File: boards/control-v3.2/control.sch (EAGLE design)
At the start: 111 parts, among them IC1 MCP23017-E/SS, J1 2-PIN-KICKERS, J3 HFW8R-1ST, J4 4-PIN-HEADER, J6 DF22-2, Q1 BSS806NH6327XTSA1, Q2 BSS806NH6327XTSA1, U1 XC3S250E-4TQG144C, U11 MCP1824T-1202E/OT, U12 MCP1824T-2502E/OT, U13 TLV70233DBVR, U4 ICM-42605, U5 SN74AHC1G125, U7 MPM3620GQV-P, U8 VND5E006ASPTR-E, X1 ASV-18.432MHZ-EJ-T

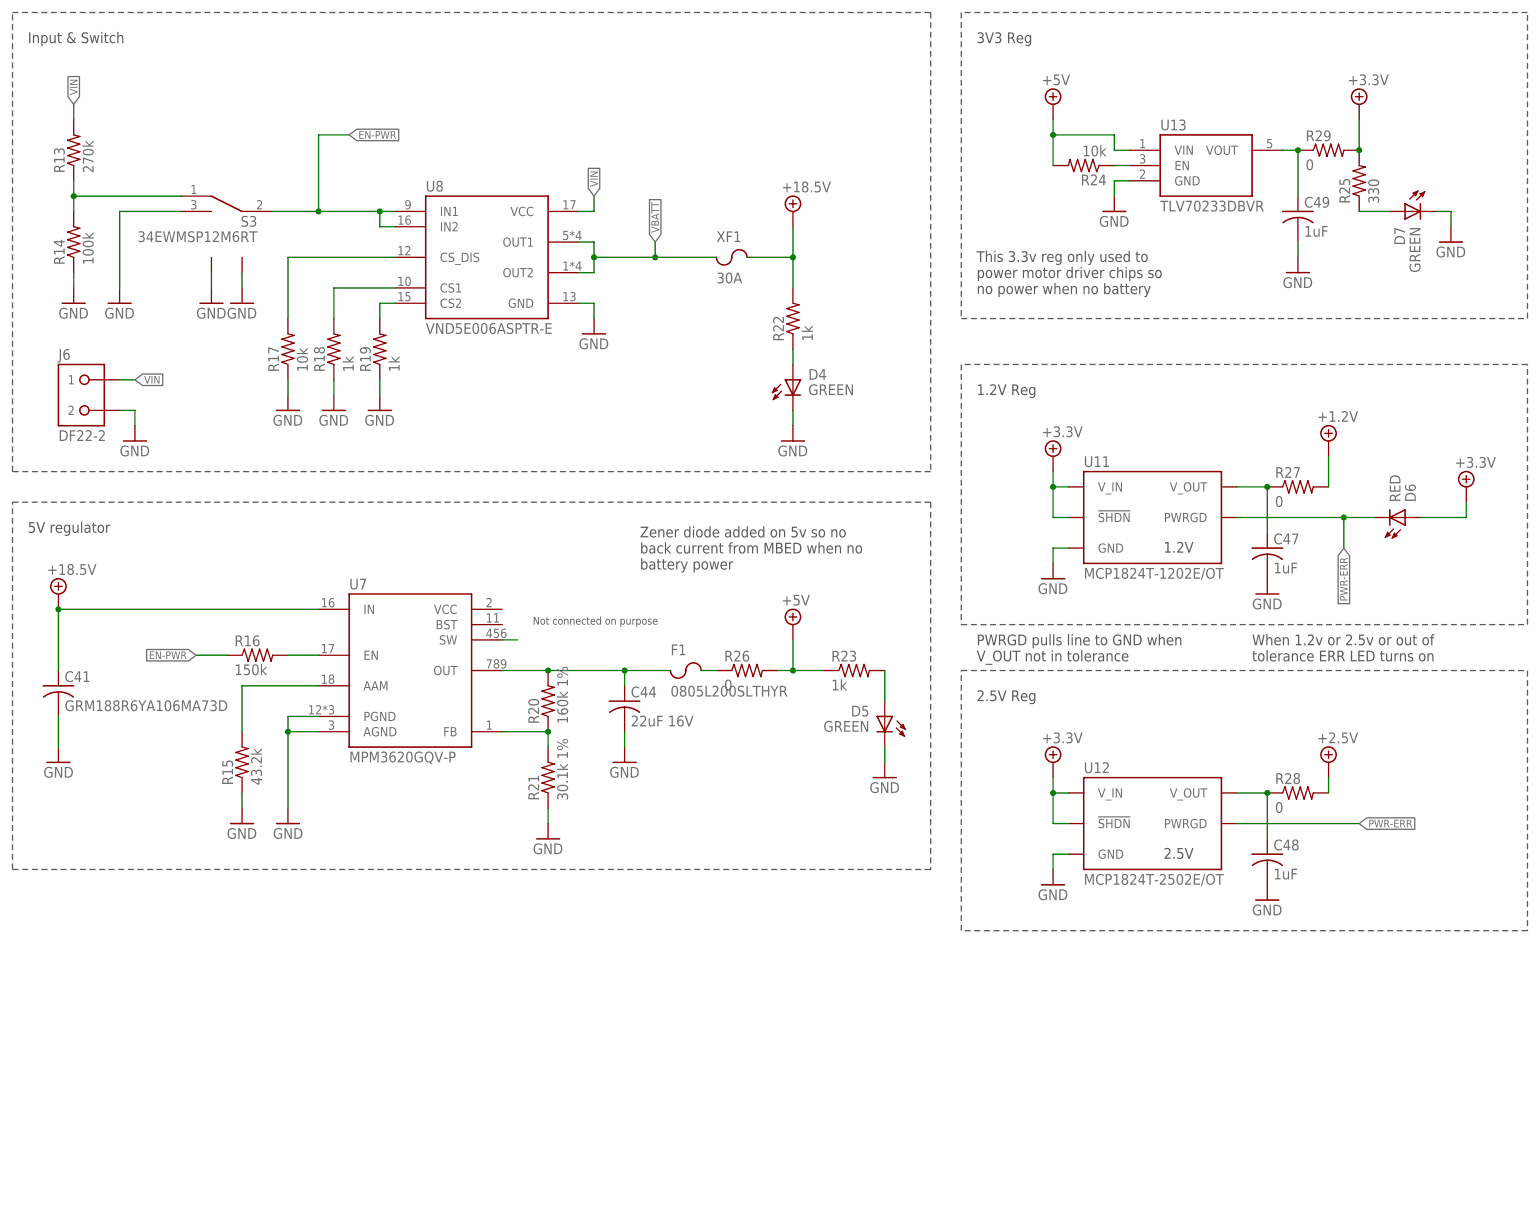
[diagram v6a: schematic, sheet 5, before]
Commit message: updated 3v3 reg
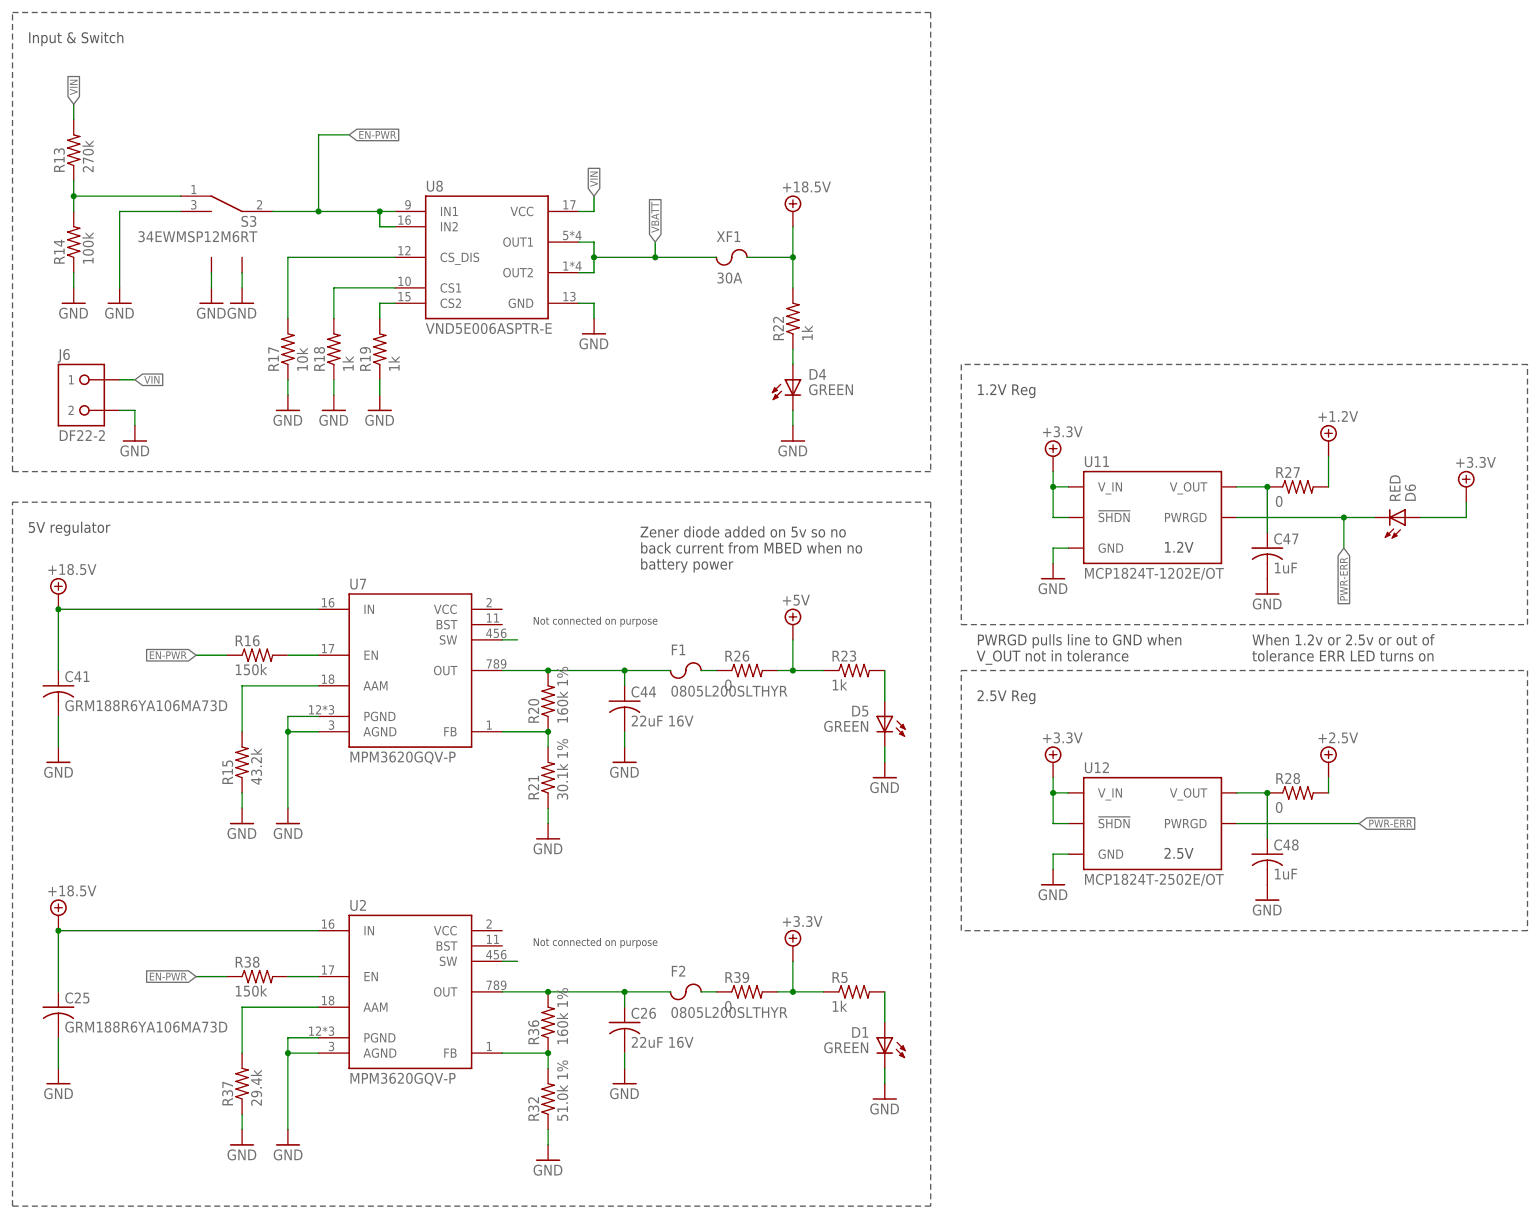
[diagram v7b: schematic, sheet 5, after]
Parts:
- removed C49: 1uF, rcl:C-USC0603
- removed D7: GREEN, RoboJackets-LEDs:LED-SMD-GREEN
- removed R24: 10k, rcl:R-US_R0603
- removed R25: 330, resistor:R-US_R0603
- removed R29: 0, resistor:R-US_R0603
- removed U13: TLV70233DBVR, RoboJackets-PowerICs:TLV70233DBVR
- added C25: GRM188R6YA106MA73D, rcl:C-USC0603
- added C26: 22uF 16V, rcl:C-USC0805
- added D1: GREEN, RoboJackets-LEDs:LED-SMD-GREEN
- added F2: 0805L200SLTHYR, RoboJackets-Fuses:CHIP_FUSE0805
- added R32: 51.0k 1%, rcl:R-US_R0603
- added R36: 160k 1%, rcl:R-US_R0603
- added R37: 29.4k, rcl:R-US_R0603
- added R38: 150k, rcl:R-US_R0603
- added R39: 0, resistor:R-US_R0603
- added R5: 1k, resistor:R-US_R0603
- added U2: MPM3620GQV-P, RoboJackets-PowerICs:MPM3620GQV-P
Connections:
- removed net +3V3-PRE: C49.1, R29.1, U13.VOUT
- removed net 3.3V-EN: R24.1, U13.EN
- removed net 3V3-LED: D7.A, R25.1
- new net +5V-FUSE1: C26.1, F2.1, R36.2, U2.OUT
- new net 5V-LED1: D1.A, R5.2
- new net AAM1: R37.2, U2.AAM
- new net EN1: R38.2, U2.EN
- new net FB1: R32.2, R36.1, U2.FB
- new net N$1: F2.2, R39.1
- new net SW1: U2.SW
- net +18.5V: now also C25.1, U2.IN
- net +3.3V: now also R39.2, R5.1; no longer R25.2, R29.2
- net +5V: no longer R24.2, U13.VIN
- net EN-PWR: now also R38.1
- net GND: now also C25.2, C26.2, D1.K, R32.1, R37.1, U2.AGND, U2.PGND; no longer C49.2, D7.K, U13.GND
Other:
- note removed: "3V3 Reg"
- note removed: "This 3.3v reg only used to power motor driver chips so no power when no battery"
